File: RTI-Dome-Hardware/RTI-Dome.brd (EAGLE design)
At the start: 80 x 71.1 mm, 31 parts, among them IC2 74LVC244

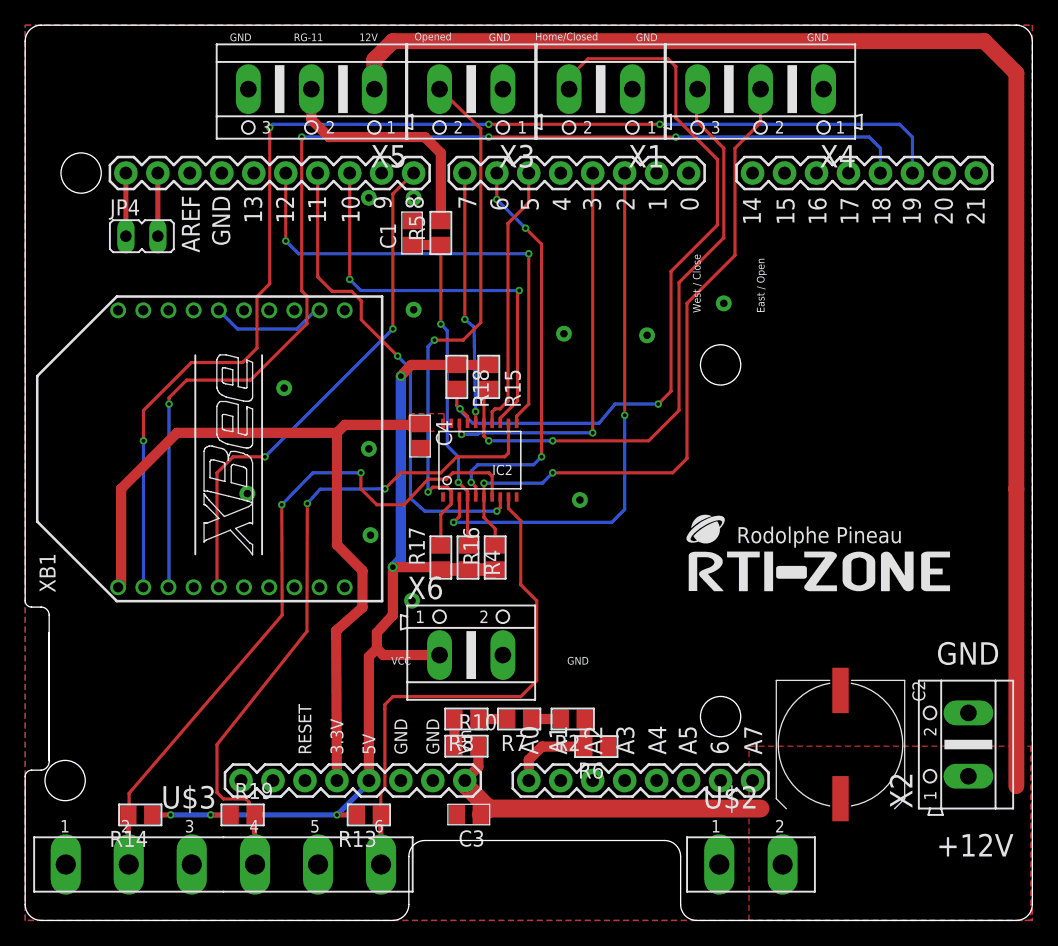
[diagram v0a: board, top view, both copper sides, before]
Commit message: Fix some components positions
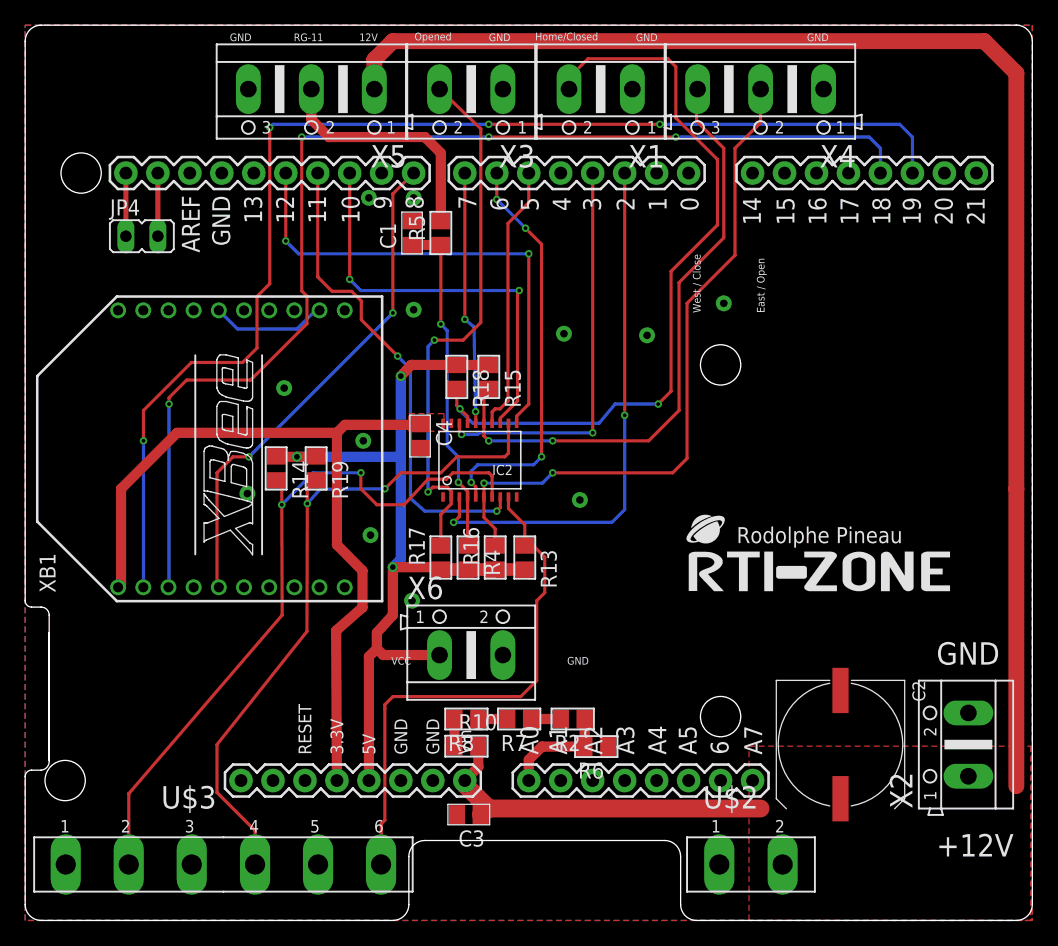
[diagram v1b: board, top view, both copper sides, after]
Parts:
- moved R14 29.6 mm to (19.9, 35.9), turned to 270 degrees
- moved R19 28.1 mm to (23.1, 35.9), turned to 270 degrees
- moved R13 23.9 mm to (39.7, 28.8), turned to 270 degrees
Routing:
- net VCC: track 75.5 -> 67.7 mm, vias 5 -> 3
- net M_EN_5V: track 55.6 -> 57.6 mm
- net M_DIR_5V: track 53.5 -> 54.6 mm
- net M_STEP_5V: track 41.2 -> 42.1 mm
- net XBEE_RESET: track 40.9 -> 40.2 mm
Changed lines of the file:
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@@
 <element name="C2" library="rti" package="UD-10X10_NICHICON" value="100uF" x="64.77" y="13.97" rot="R270"/>
 <element name="IC2" library="rti" package="TSSOP20" value="74LVC244" x="36.83" y="36.83" rot="R90"/>
-<element name="R13" library="rti" package="R0805" value="1K" x="27.305" y="8.382" rot="R180"/>
-<element name="R14" library="rti" package="R0805" value="1K" x="9.144" y="8.382" rot="R180"/>
+<element name="R13" library="rti" package="R0805" value="1K" x="39.6875" y="28.829" rot="R270"/>
+<element name="R14" library="rti" package="R0805" value="1K" x="19.939" y="35.90925" rot="R270"/>
 <element name="R15" library="rti" package="R0805" value="4.7K" x="36.83" y="43.18" rot="R270"/>
 <element name="R16" library="rti" package="R0805" value="4.7K" x="37.338" y="28.829" rot="R90"/>
 <element name="R17" library="rti" package="R0805" value="4.7K" x="33.02" y="28.829" rot="R90"/>
 <element name="R18" library="rti" package="R0805" value="4.7K" x="34.29" y="43.18" rot="R270"/>
-<element name="R19" library="rti" package="R0805" value="1K" x="17.272" y="8.382"/>
+<element name="R19" library="rti" package="R0805" value="1K" x="23.114" y="35.90925" rot="R270"/>
 <element name="R6" library="rti" package="R0805" value="100K 0.1%" x="45.37075" y="13.81125" rot="R180"/>
 <element name="R7" library="rti" package="R0805" value="100K 0.1%" x="39.243" y="16.002" rot="R180"/>
@@
 <contactref element="X2" pad="2"/>
 <via x="44.069" y="33.401" extent="1-16" drill="0.6" diameter="1.27"/>
-<via x="27.305" y="37.465" extent="1-16" drill="0.6" diameter="1.27"/>
+<via x="26.8605" y="38.1" extent="1-16" drill="0.6" diameter="1.27"/>
 <via x="42.799" y="46.609" extent="1-16" drill="0.6" diameter="1.27"/>
 <via x="30.734" y="25.4" extent="1-16" drill="0.6" diameter="1.27"/>
@@
 <contactref element="R13" pad="1"/>
 <contactref element="IC2" pad="P$9"/>
-<wire x1="28.2702" y1="4.445" x2="28.255" y2="4.445" width="0.4064" layer="1"/>
-<wire x1="28.255" y1="4.445" x2="28.255" y2="8.382" width="0.4064" layer="1"/>
 <wire x1="38.395" y1="33.64" x2="38.395" y2="32.725" width="0.254" layer="1"/>
-<wire x1="38.395" y1="32.725" x2="39.37" y2="31.75" width="0.254" layer="1"/>
-<wire x1="28.255" y1="8.382" x2="28.255" y2="10.1575" width="0.254" layer="1"/>
-<wire x1="28.255" y1="10.1575" x2="28.575" y2="10.4775" width="0.254" layer="1"/>
 <wire x1="28.575" y1="10.4775" x2="28.575" y2="16.8275" width="0.254" layer="1"/>
 <wire x1="28.575" y1="16.8275" x2="28.575" y2="17.145" width="0.254" layer="1"/>
@@
 <wire x1="39.37" y1="17.78" x2="40.64" y2="19.05" width="0.254" layer="1"/>
 <wire x1="40.64" y1="19.05" x2="40.64" y2="25.4" width="0.254" layer="1"/>
-<wire x1="40.64" y1="25.4" x2="39.37" y2="26.67" width="0.254" layer="1"/>
-<wire x1="39.37" y1="26.67" x2="39.37" y2="31.75" width="0.254" layer="1"/>
+<wire x1="38.395" y1="32.725" x2="39.6875" y2="31.4325" width="0.254" layer="1"/>
+<wire x1="39.6875" y1="31.4325" x2="39.6875" y2="29.779" width="0.254" layer="1"/>
+<wire x1="39.6875" y1="29.779" x2="40.35675" y2="29.779" width="0.254" layer="1"/>
+<wire x1="40.35675" y1="29.779" x2="41.275" y2="28.86075" width="0.254" layer="1"/>
+<wire x1="41.275" y1="28.86075" x2="41.275" y2="26.035" width="0.254" layer="1"/>
+<wire x1="41.275" y1="26.035" x2="40.64" y2="25.4" width="0.254" layer="1"/>
+<wire x1="28.575" y1="10.4775" x2="28.575" y2="7.96925" width="0.254" layer="1"/>
+<wire x1="28.575" y1="7.96925" x2="28.28925" y2="7.6835" width="0.254" layer="1"/>
+<wire x1="28.28925" y1="7.6835" x2="28.28925" y2="4.46405" width="0.254" layer="1"/>
+<wire x1="28.28925" y1="4.46405" x2="28.2702" y2="4.445" width="0.254" layer="1"/>
 </signal>
 <signal name="M_DIR_5V">
 <contactref element="U$3" pad="4"/>
 <contactref element="R19" pad="2"/>
-<wire x1="17.747" y1="8.857" x2="18.222" y2="8.382" width="0.254" layer="1"/>
 <contactref element="IC2" pad="P$12"/>
-<wire x1="18.2626" y1="4.445" x2="18.222" y2="4.445" width="0.4064" layer="1"/>
-<wire x1="18.222" y1="4.445" x2="18.222" y2="8.382" width="0.4064" layer="1"/>
 <wire x1="38.395" y1="39.49" x2="38.395" y2="37.125" width="0.254" layer="1"/>
 <wire x1="38.395" y1="37.125" x2="38.1" y2="36.83" width="0.254" layer="1"/>
@@
 <wire x1="22.38375" y1="22.95525" x2="15.24" y2="13.97" width="0.254" layer="1"/>
 <wire x1="15.24" y1="13.97" x2="15.24" y2="10.16" width="0.254" layer="1"/>
-<wire x1="15.24" y1="10.16" x2="15.748" y2="9.652" width="0.254" layer="1"/>
-<wire x1="15.748" y1="9.652" x2="17.526" y2="9.652" width="0.254" layer="1"/>
-<wire x1="17.526" y1="9.652" x2="17.78" y2="9.398" width="0.254" layer="1"/>
-<wire x1="17.78" y1="9.398" x2="17.78" y2="8.89" width="0.254" layer="1"/>
-<wire x1="17.78" y1="8.89" x2="17.747" y2="8.857" width="0.254" layer="1"/>
+<wire x1="23.114" y1="34.95925" x2="22.4155" y2="34.26075" width="0.254" layer="1"/>
+<wire x1="22.4155" y1="34.26075" x2="22.4155" y2="33.11525" width="0.254" layer="1"/>
+<wire x1="15.24" y1="10.16" x2="18.2626" y2="7.1374" width="0.254" layer="1"/>
+<wire x1="18.2626" y1="7.1374" x2="18.2626" y2="4.445" width="0.254" layer="1"/>
 </signal>
 <signal name="M_EN_5V">
@@
 <contactref element="R14" pad="2"/>
 <contactref element="IC2" pad="P$7"/>
-<wire x1="8.2296" y1="4.445" x2="8.194" y2="4.445" width="0.4064" layer="1"/>
-<wire x1="8.194" y1="4.445" x2="8.194" y2="8.382" width="0.4064" layer="1"/>
 <wire x1="37.095" y1="33.64" x2="37.095" y2="35.295" width="0.254" layer="1"/>
 <wire x1="37.095" y1="35.295" x2="36.83" y2="35.56" width="0.254" layer="1"/>
@@
 <wire x1="20.3835" y1="33.02" x2="20.41525" y2="24.257" width="0.254" layer="1"/>
 <wire x1="20.41525" y1="24.257" x2="8.255" y2="10.0965" width="0.254" layer="1"/>
-<wire x1="8.255" y1="10.0965" x2="8.255" y2="8.443" width="0.254" layer="1"/>
-<wire x1="8.255" y1="8.443" x2="8.194" y2="8.382" width="0.254" layer="1"/>
+<wire x1="19.939" y1="34.95925" x2="20.3835" y2="34.51475" width="0.254" layer="1"/>
+<wire x1="20.3835" y1="34.51475" x2="20.3835" y2="33.02" width="0.254" layer="1"/>
+<wire x1="8.255" y1="10.0965" x2="8.2296" y2="10.0711" width="0.254" layer="1"/>
+<wire x1="8.2296" y1="10.0711" x2="8.2296" y2="4.445" width="0.254" layer="1"/>
 </signal>
 <signal name="RG-11-IN_EXT">
@@
 <contactref element="R19" pad="1"/>
 <contactref element="R4" pad="2"/>
-<wire x1="27.305" y1="11.1125" x2="27.305" y2="10.922" width="0.4064" layer="16"/>
-<wire x1="27.305" y1="10.922" x2="24.765" y2="8.382" width="0.4064" layer="16"/>
-<wire x1="24.765" y1="8.382" x2="14.732" y2="8.382" width="0.4064" layer="16"/>
-<via x="11.557" y="8.382" extent="1-16" drill="0.3"/>
-<wire x1="14.732" y1="8.382" x2="11.557" y2="8.382" width="0.4064" layer="16"/>
-<wire x1="11.557" y1="8.382" x2="10.094" y2="8.382" width="0.4064" layer="1"/>
-<wire x1="16.322" y1="8.382" x2="14.732" y2="8.382" width="0.4064" layer="1"/>
-<via x="14.732" y="8.382" extent="1-16" drill="0.3"/>
-<via x="24.765" y="8.382" extent="1-16" drill="0.3"/>
-<wire x1="26.355" y1="8.382" x2="24.765" y2="8.382" width="0.4064" layer="1"/>
 <wire x1="33.02" y1="27.879" x2="35.179" y2="27.879" width="1.016" layer="1"/>
 <wire x1="35.179" y1="27.879" x2="37.338" y2="27.879" width="1.016" layer="1"/>
@@
 <wire x1="30.6705" y1="44.1325" x2="29.845" y2="43.2435" width="0.8128" layer="1"/>
 <via x="29.845" y="43.2435" extent="1-16" drill="0.45" diameter="0.8128"/>
-<wire x1="29.845" y1="43.2435" x2="29.845" y2="28.702" width="0.8128" layer="16"/>
+<wire x1="29.845" y1="43.2435" x2="29.845" y2="36.83" width="0.8128" layer="16"/>
+<wire x1="29.845" y1="36.83" x2="29.845" y2="28.702" width="0.8128" layer="16"/>
 <wire x1="29.845" y1="28.702" x2="29.21" y2="28.067" width="0.8128" layer="16"/>
 <via x="29.21" y="28.067" extent="1-16" drill="0.45" diameter="0.8128"/>
@@
 <wire x1="32.9184" y1="21.082" x2="28.448" y2="21.082" width="0.8128" layer="1"/>
 <wire x1="28.448" y1="21.082" x2="27.94" y2="21.59" width="0.8128" layer="1"/>
+<wire x1="39.6875" y1="27.879" x2="37.338" y2="27.879" width="1.016" layer="1"/>
+<wire x1="23.114" y1="36.85925" x2="23.08475" y2="36.83" width="0.4064" layer="1"/>
+<wire x1="23.08475" y1="36.83" x2="21.59" y2="36.83" width="0.8128" layer="1"/>
+<via x="21.59" y="36.83" extent="1-16" drill="0.45" diameter="0.8128"/>
+<wire x1="21.59" y1="36.83" x2="29.845" y2="36.83" width="0.8128" layer="16"/>
+<wire x1="19.939" y1="36.85925" x2="19.96825" y2="36.83" width="0.4064" layer="1"/>
+<wire x1="19.96825" y1="36.83" x2="21.59" y2="36.83" width="0.8128" layer="1"/>
 </signal>
 <signal name="N$2">
@@
 <signal name="XBEE_RESET">
 <contactref element="XB1" pad="5"/>
-<via x="29.21" y="46.99" extent="1-16" drill="0.3"/>
-<wire x1="29.21" y1="46.99" x2="19.05" y2="36.83" width="0.254" layer="16"/>
-<via x="19.05" y="36.83" extent="1-16" drill="0.3"/>
-<wire x1="19.05" y1="36.83" x2="16.51" y2="36.83" width="0.254" layer="1"/>
+<via x="29.21" y="48.26" extent="1-16" drill="0.3"/>
+<wire x1="29.21" y1="48.26" x2="17.78" y2="36.83" width="0.254" layer="16"/>
+<via x="17.78" y="36.83" extent="1-16" drill="0.3"/>
+<wire x1="17.78" y1="36.83" x2="16.51" y2="36.83" width="0.254" layer="1"/>
 <wire x1="16.51" y1="36.83" x2="15.24" y2="35.56" width="0.254" layer="1"/>
 <wire x1="15.24" y1="35.56" x2="15.24" y2="26.608" width="0.254" layer="1"/>
 <wire x1="15.24" y1="26.608" x2="15.383" y2="26.465" width="0.254" layer="1"/>
-<wire x1="29.21" y1="46.99" x2="29.21" y2="57.7215" width="0.254" layer="1"/>
+<wire x1="29.21" y1="48.26" x2="29.21" y2="57.7215" width="0.254" layer="1"/>
 <wire x1="29.21" y1="57.7215" x2="30.861" y2="59.3725" width="0.254" layer="1"/>
 <contactref element="PCB1" pad="8"/>

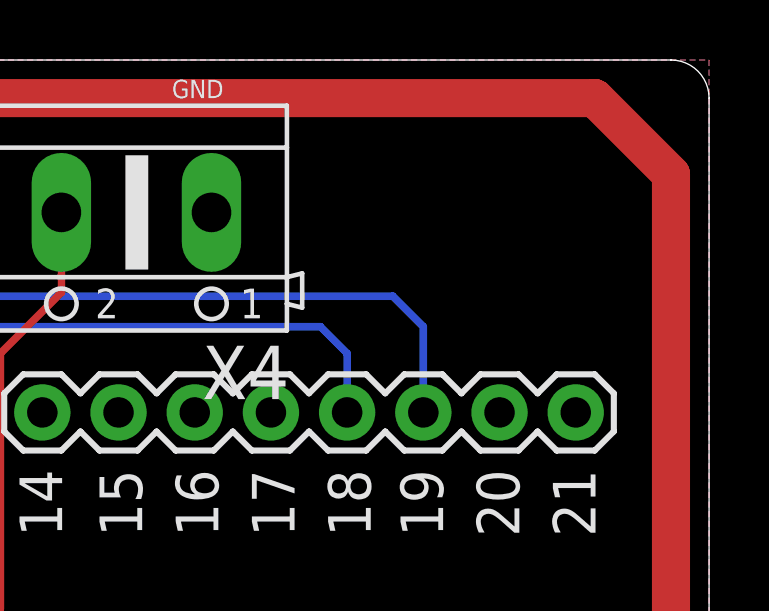
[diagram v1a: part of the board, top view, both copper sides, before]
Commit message: Stop interrupt in motor disable code.
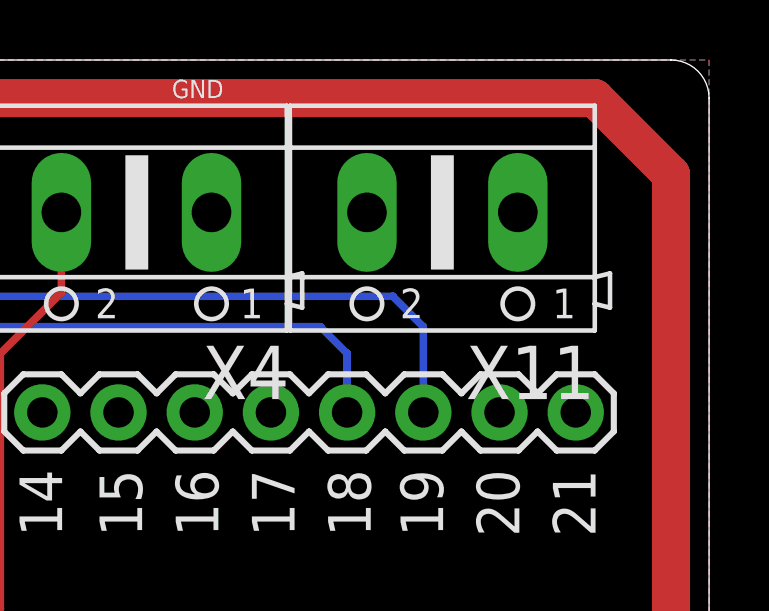
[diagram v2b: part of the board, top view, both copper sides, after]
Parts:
- added X11: (no value), con-ptr500:AK500/2
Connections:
- new net AT_PARK_PIN: PCB1.A5, X11.1
- new net AT_PARK_PIN_LOOP: PCB1.A4, X11.2
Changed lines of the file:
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@@
 <element name="R2" library="rti" package="R0805" value="100K 0.1%" x="43.4975" y="16.002" rot="R180"/>
 <element name="C3" library="rti" package="C0805" value="10uF" x="35.2425" y="8.41375" rot="R180"/>
+<element name="X11" library="con-ptr500" package="AK500/2" value="" x="71.12" y="66.04" rot="R180">
+<attribute name="MF" value="" x="71.12" y="66.04" size="1.778" layer="27" rot="R180" display="off"/>
+<attribute name="OC_NEWARK" value="unknown" x="71.12" y="66.04" size="1.778" layer="27" rot="R180" display="off"/>
+<attribute name="MPN" value="" x="71.12" y="66.04" size="1.778" layer="27" rot="R180" display="off"/>
+<attribute name="OC_FARNELL" value="unknown" x="71.12" y="66.04" size="1.778" layer="27" rot="R180" display="off"/>
+</element>
 </elements>
 <signals>
@@
 <wire x1="40.193" y1="16.002" x2="42.5475" y2="16.002" width="0.8128" layer="1"/>
 </signal>
+<signal name="AT_PARK_PIN_LOOP">
+<contactref element="X11" pad="2"/>
+<contactref element="PCB1" pad="A4"/>
+<wire x1="68.6054" y1="66.04" x2="50.165" y2="11.1125" width="0" layer="19" extent="1-1"/>
+</signal>
+<signal name="AT_PARK_PIN">
+<contactref element="X11" pad="1"/>
+<contactref element="PCB1" pad="A5"/>
+<wire x1="73.6346" y1="66.04" x2="52.705" y2="11.1125" width="0" layer="19" extent="1-1"/>
+</signal>
 </signals>
